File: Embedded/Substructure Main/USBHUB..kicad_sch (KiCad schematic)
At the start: 19 parts, among them U8 USB2513B_Bi, Y1 TSX-3225 24MF18X-C0

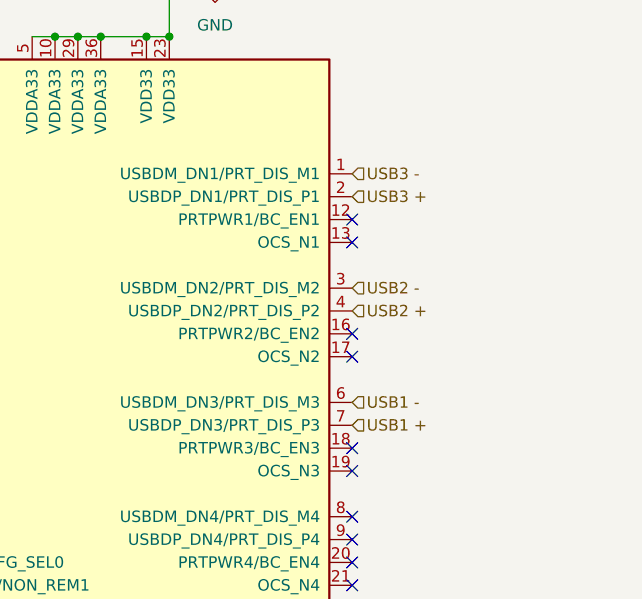
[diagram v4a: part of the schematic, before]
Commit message: Added Routing for USB lanes, power & other data lanes
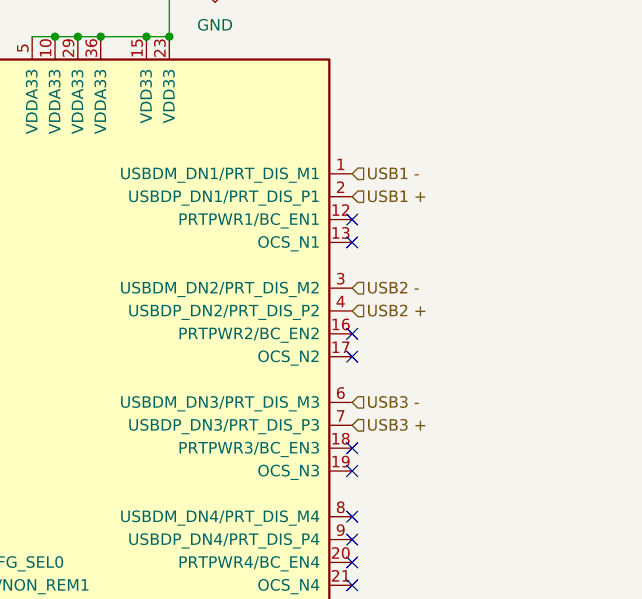
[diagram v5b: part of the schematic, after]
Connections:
- net USB1 +: now also U8.2 (USBDP_DN1/PRT_DIS_P1); no longer U8.7 (USBDP_DN3/PRT_DIS_P3)
- net USB1 -: now also U8.1 (USBDM_DN1/PRT_DIS_M1); no longer U8.6 (USBDM_DN3/PRT_DIS_M3)
- net USB3 +: now also U8.7 (USBDP_DN3/PRT_DIS_P3); no longer U8.2 (USBDP_DN1/PRT_DIS_P1)
- net USB3 -: now also U8.6 (USBDM_DN3/PRT_DIS_M3); no longer U8.1 (USBDM_DN1/PRT_DIS_M1)
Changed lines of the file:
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@@
 	(hierarchical_label "USB3 -"
 		(shape input)
-		(at 218.44 76.2 0)
+		(at 218.44 101.6 0)
 		(effects
 			(font
@@
 	(hierarchical_label "USB1 +"
 		(shape input)
-		(at 218.44 104.14 0)
+		(at 218.44 78.74 0)
 		(effects
 			(font
@@
 	(hierarchical_label "USB1 -"
 		(shape input)
-		(at 218.44 101.6 0)
+		(at 218.44 76.2 0)
 		(effects
 			(font
@@
 	(hierarchical_label "USB3 +"
 		(shape input)
-		(at 218.44 78.74 0)
+		(at 218.44 104.14 0)
 		(effects
 			(font
